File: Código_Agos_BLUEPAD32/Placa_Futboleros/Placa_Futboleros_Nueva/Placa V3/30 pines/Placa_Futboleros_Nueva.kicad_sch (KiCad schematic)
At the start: 17 parts, among them J1 BAT, J2 Motor_Izq_Adelante, J3 Motor_Izq_Atras, J4 Motor_Der_Adelante, J5 Motor_Der_Atras, U1 LM7805_TO220, U3 DRV8833, U4 DRV8833, U5 ESP32-DEVKIT-V1

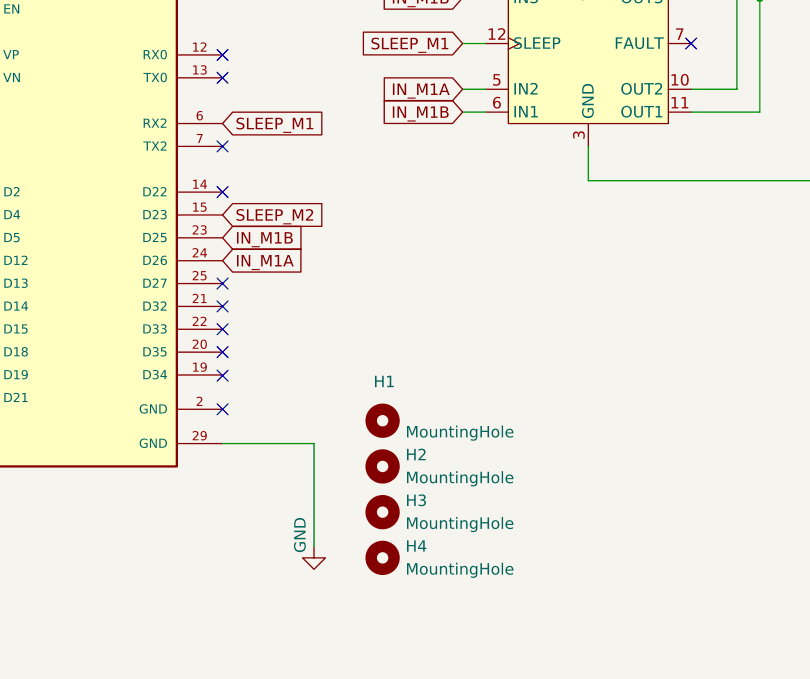
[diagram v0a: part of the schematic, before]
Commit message: Idea e Implementación Futura para Placa 30 pines V3
Se agrega un divisor resistivo de las baterías al ADC para monitoreo
y lectura del voltaje de las baterías para mnostrar en la web cuando
se active el AP; con el fin de también poseer un historial de mediciones
y calcular la cantidad de partidos.

También conviene para regular el PWM en función del voltaje
recibido para mantener la potencia en los motores.
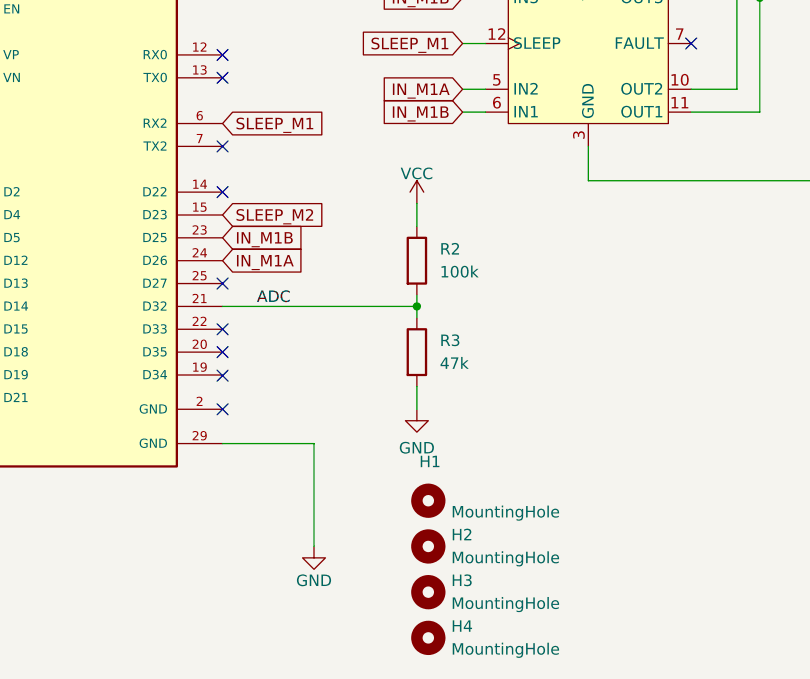
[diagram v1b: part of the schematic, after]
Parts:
- added R2: 100k, Resistor_THT:R_Axial_DIN0207_L6.3mm_D2.5mm_P10.16mm_Horizontal, symbol Device:R
- added R3: 47k, Resistor_THT:R_Axial_DIN0207_L6.3mm_D2.5mm_P10.16mm_Horizontal, symbol Device:R
- U5: footprint ESP32-DEVKIT-V1:MODULE_ESP32_DEVKIT_V1 -> MODULE_ESP32_DEVKIT_V1:MODULE_ESP32_DEVKIT_V1
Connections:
- net GND: now also R3.2
- net VCC: now also R2.1
- net ADC: now reaches U5.21 (D32)
- net ADC: now also R2.2, R3.1
- no-connect marks 21 -> 20
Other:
- moved on the sheet: H1, H2, H3, H4
